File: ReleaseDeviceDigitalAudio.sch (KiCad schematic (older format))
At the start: 7 parts, among them J1 Conn_02x10_Counter_Clockwise

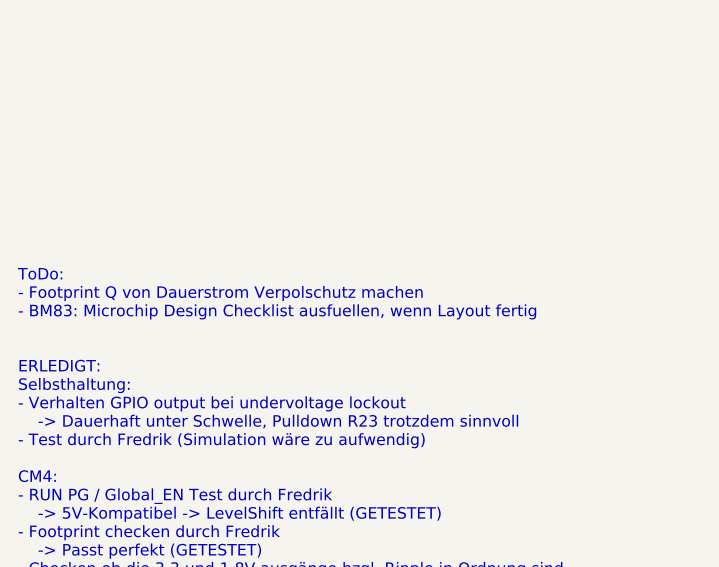
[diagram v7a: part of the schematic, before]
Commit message: - Galvanische Trennung zu KFZ abgeschlossen
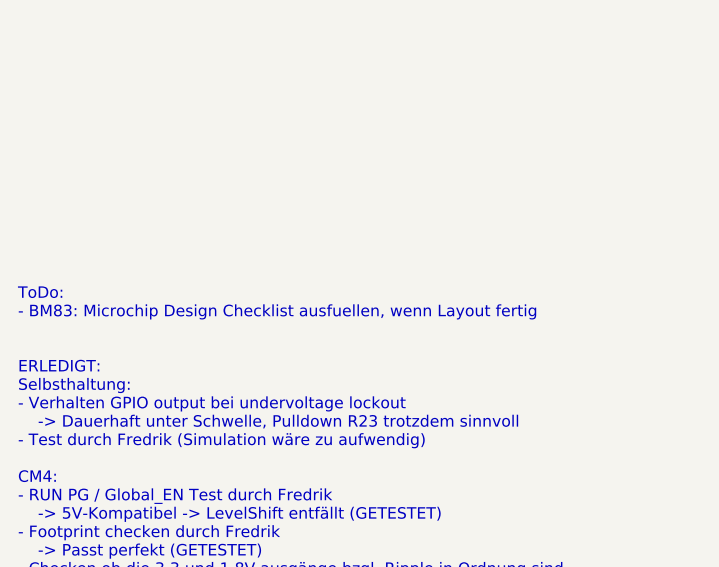
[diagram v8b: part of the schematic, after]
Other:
- note added: "ToDo: \n- BM83: Microchip Design Checklist ausfuellen, wenn Layout fertig\n\n\nERLEDIGT:\nSelbsthaltung:\n- Verhalten GPIO output bei undervoltage lockout \n -> Dauerhaft unter Schwelle, Pulldown R23 trotzdem sinnvoll\n- Test durch Fredrik (Simulation wäre zu aufwendig)\n\nCM4: \n- RUN PG / Global_EN Test durch Fredrik\n -> 5V-Kompatibel -> LevelShift entfällt (GETESTET)\n- Footprint checken durc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"
- note removed: "ToDo: \n- Footprint Q von Dauerstrom Verpolschutz machen\n- BM83: Microchip Design Checklist ausfuellen, wenn Layout fertig\n\n\nERLEDIGT:\nSelbsthaltung:\n- Verhalten GPIO output bei undervoltage lockout \n -> Dauerhaft unter Schwelle, Pulldown R23 trotzdem sinnvoll\n- Test durch Fredrik (Simulation wäre zu aufwendig)\n\nCM4: \n- RUN PG / Global_EN Test durch Fredrik\n -> 5V-Kompatibel -> LevelS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"
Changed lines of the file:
@@
 	1    0    0    -1
 $EndComp
-Text Notes 800  7100 0    50   ~ 0
-ToDo: \n- Footprint Q von Dauerstrom Verpolschutz machen\n- BM83: Microchip Design Checklist ausfuellen, wenn Layout fertig\n\n\nERLEDIGT:\nSelbsthaltung:\n- Verhalten GPIO output bei undervoltage lockout \n    -> Dauerhaft unter Schwelle, Pulldown R23 trotzdem sinnvoll\n- Test durch Fredrik (Simulation wäre zu aufwendig)\n\nCM4: \n- RUN PG / Global_EN Test durch Fredrik\n    -> 5V-Kompatibel -> LevelShift entfällt (GETESTET)\n- Footprint checken durch Fredrik\n    -> Passt perfekt (GETESTET)\n- Checken ob die 3,3 und 1,8V ausgänge bzgl. Ripple in Ordnung sind\n    -> Für MAX98089 ausreichend, Oszi fehlt, daher keine genauen Daten\n- Schaltfrequenz onboard Regler\n    -> 1 - 2.1 MHz (abhängig von Config)\n\nBM83\n- Unused Pin Connections nicht beschrieben \n    -> floating lassen und später Prüfung mit Design check\n- Temperatur Messung HW seitig implementieren\n   -> Fredrik kümmert sich ggf. um SW Implementierung, etc.\n- MFB wird noch getestet durch Fredrik  \n   -> nicht benötigt, da Power On/Off per UART konfigurierbar\n- MCLK-Ausgang implementiert\n- Ersetzen durch Modell mit automotive Zulassung?\n   -> Nein weiter so mit 4Layers Aussage zur Typgenehmigung\n\nMAX98089:\n- LDO für MAX98089? \n    - Test: Stromversorgung über CM: kein Noise, Load unerheblich\n- Config: Voice vs. Music filter: Done\n- MCLK-Eingang implementiert\n\nATmega:\n- Wozu 10k R an PWM Ausgang?\n   -> 1V macht Vollaussteuerung\n        Fredrik klärt PWM Frequenz, Auflöung und Eingangs-R des Zeigers\n        -> Vollausst. bei 0.22V, 0.5-1k R_innen -> 15k Vorwiderstand (GETESTET)\n        -> PER=100 -> 0,05V-Schritte, f=100kHz\n- Programmierbeschaltung ohne Reset?\n    -> check durch Fredrik -> Reset nicht benötigt\n- int. OSC checken bzgl. Kalwerte und UART Baudrate\n    -> betrifft nur SW, Bearbeitung durch Fredrik\n- Auslegung Spannungsteiler mit LDR\n    -> Standard 10k\n\nAllgemeines: \n- Levelshift prüfen (Zuordnung RX/TX)\n- Signalzuordungen I2C / I2S / UART checken\n- Abschaltung UI Board implementieren \n   (SW6 soll 5V von UI Board schalten, LED_ON alternierend dazu)\n- Zündung nur 1pol anschließen? -> kein Verpolschutz notwendig\n  (Optokoppler Eingang verträgt nur 5V reverse…)\n    -> Ja, mit 3 poligen Kombistecker\n- Auslegung Vorwiderstände an reale LEDs\n- Auswahl Steckverbinder Analog Audio\n- Auswahl Steckverbinder KFZ (Dauerstrom / Zündung) 3Pol\n- Battery Holder auf SMD Variante CR2032 geändert
 Wire Wire Line
 	9650 2400 10050 2400
@@
 Wire Wire Line
 	13000 2200 13000 2300
+Text Notes 800  7100 0    50   ~ 0
+ToDo: \n- BM83: Microchip Design Checklist ausfuellen, wenn Layout fertig\n\n\nERLEDIGT:\nSelbsthaltung:\n- Verhalten GPIO output bei undervoltage lockout \n    -> Dauerhaft unter Schwelle, Pulldown R23 trotzdem sinnvoll\n- Test durch Fredrik (Simulation wäre zu aufwendig)\n\nCM4: \n- RUN PG / Global_EN Test durch Fredrik\n    -> 5V-Kompatibel -> LevelShift entfällt (GETESTET)\n- Footprint checken durch Fredrik\n    -> Passt perfekt (GETESTET)\n- Checken ob die 3,3 und 1,8V ausgänge bzgl. Ripple in Ordnung sind\n    -> Für MAX98089 ausreichend, Oszi fehlt, daher keine genauen Daten\n- Schaltfrequenz onboard Regler\n    -> 1 - 2.1 MHz (abhängig von Config)\n\nBM83\n- Unused Pin Connections nicht beschrieben \n    -> floating lassen und später Prüfung mit Design check\n- Temperatur Messung HW seitig implementieren\n   -> Fredrik kümmert sich ggf. um SW Implementierung, etc.\n- MFB wird noch getestet durch Fredrik  \n   -> nicht benötigt, da Power On/Off per UART konfigurierbar\n- MCLK-Ausgang implementiert\n- Ersetzen durch Modell mit automotive Zulassung?\n   -> Nein weiter so mit 4Layers Aussage zur Typgenehmigung\n\nMAX98089:\n- LDO für MAX98089? \n    - Test: Stromversorgung über CM: kein Noise, Load unerheblich\n- Config: Voice vs. Music filter: Done\n- MCLK-Eingang implementiert\n\nATmega:\n- Wozu 10k R an PWM Ausgang?\n   -> 1V macht Vollaussteuerung\n        Fredrik klärt PWM Frequenz, Auflöung und Eingangs-R des Zeigers\n        -> Vollausst. bei 0.22V, 0.5-1k R_innen -> 15k Vorwiderstand (GETESTET)\n        -> PER=100 -> 0,05V-Schritte, f=100kHz\n- Programmierbeschaltung ohne Reset?\n    -> check durch Fredrik -> Reset nicht benötigt\n- int. OSC checken bzgl. Kalwerte und UART Baudrate\n    -> betrifft nur SW, Bearbeitung durch Fredrik\n- Auslegung Spannungsteiler mit LDR\n    -> Standard 10k\n\nAllgemeines: \n- Levelshift prüfen (Zuordnung RX/TX)\n- Signalzuordungen I2C / I2S / UART checken\n- Abschaltung UI Board implementieren \n   (SW6 soll 5V von UI Board schalten, LED_ON alternierend dazu)\n- Zündung nur 1pol anschließen? -> kein Verpolschutz notwendig\n  (Optokoppler Eingang verträgt nur 5V reverse…)\n    -> Ja, mit 3 poligen Kombistecker\n- Auslegung Vorwiderstände an reale LEDs\n- Auswahl Steckverbinder Analog Audio\n- Auswahl Steckverbinder KFZ (Dauerstrom / Zündung) 3Pol\n- Battery Holder auf SMD Variante CR2032 geändert
 $EndSCHEMATC
